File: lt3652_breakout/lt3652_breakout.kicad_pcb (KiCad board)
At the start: 2 copper layers, 37 parts, among them CON1 SLR PNL, U1 LT3652

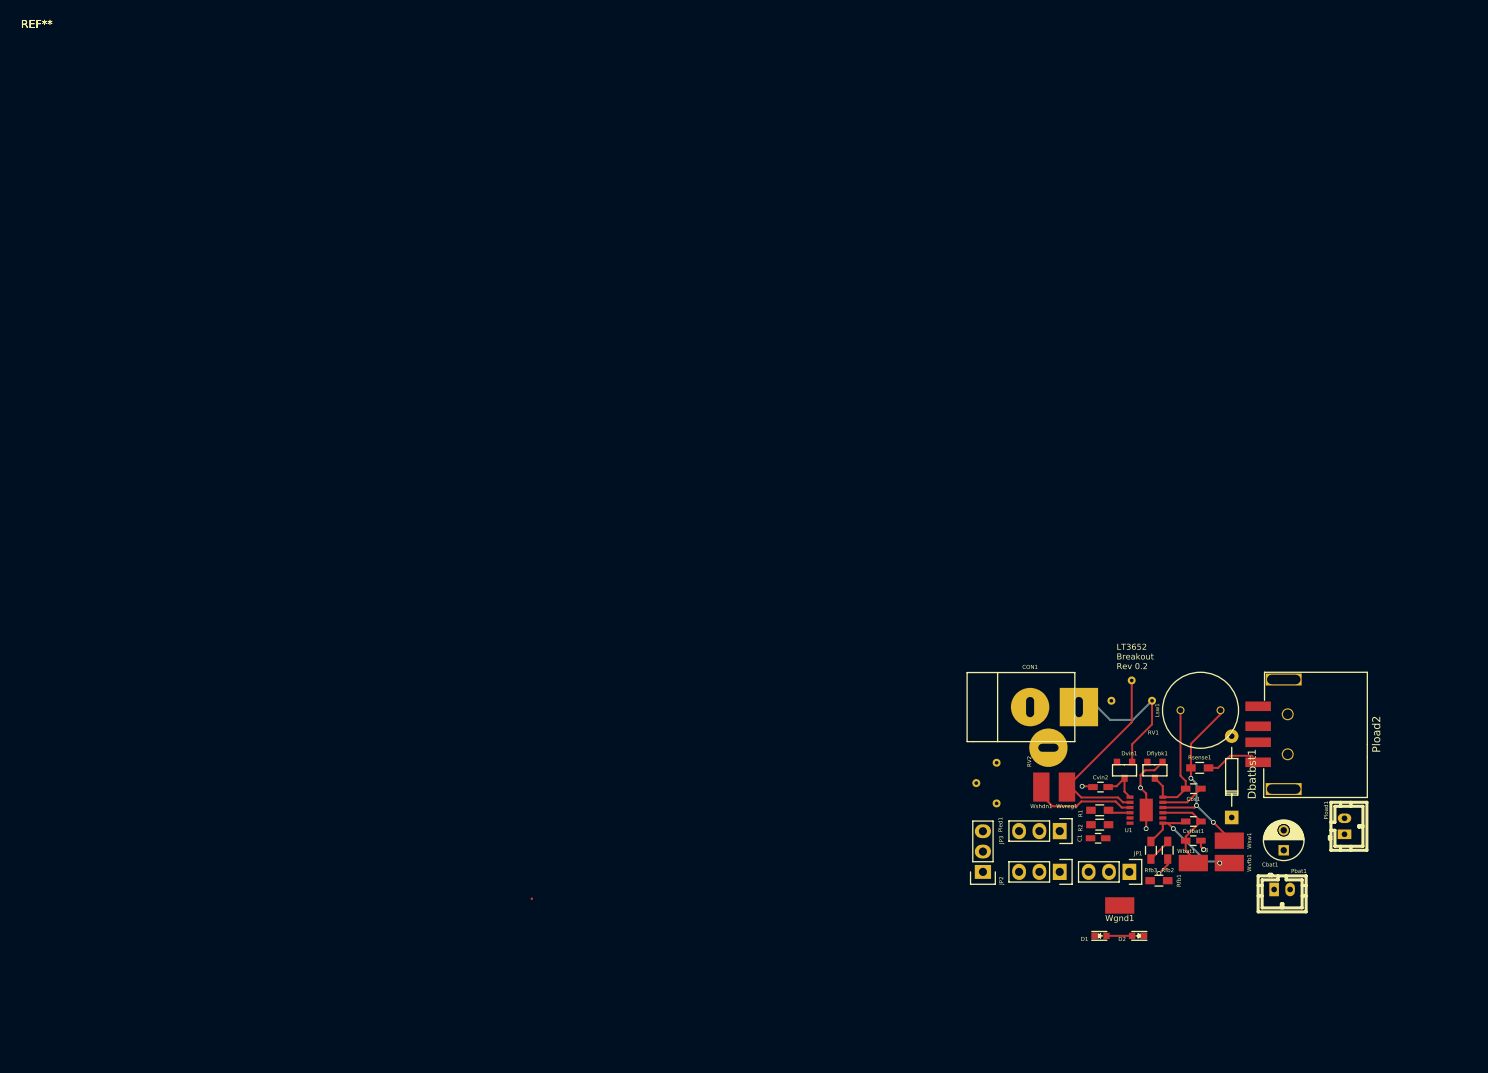
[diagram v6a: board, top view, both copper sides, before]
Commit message: Relaid pcb to the size of the box that will house it
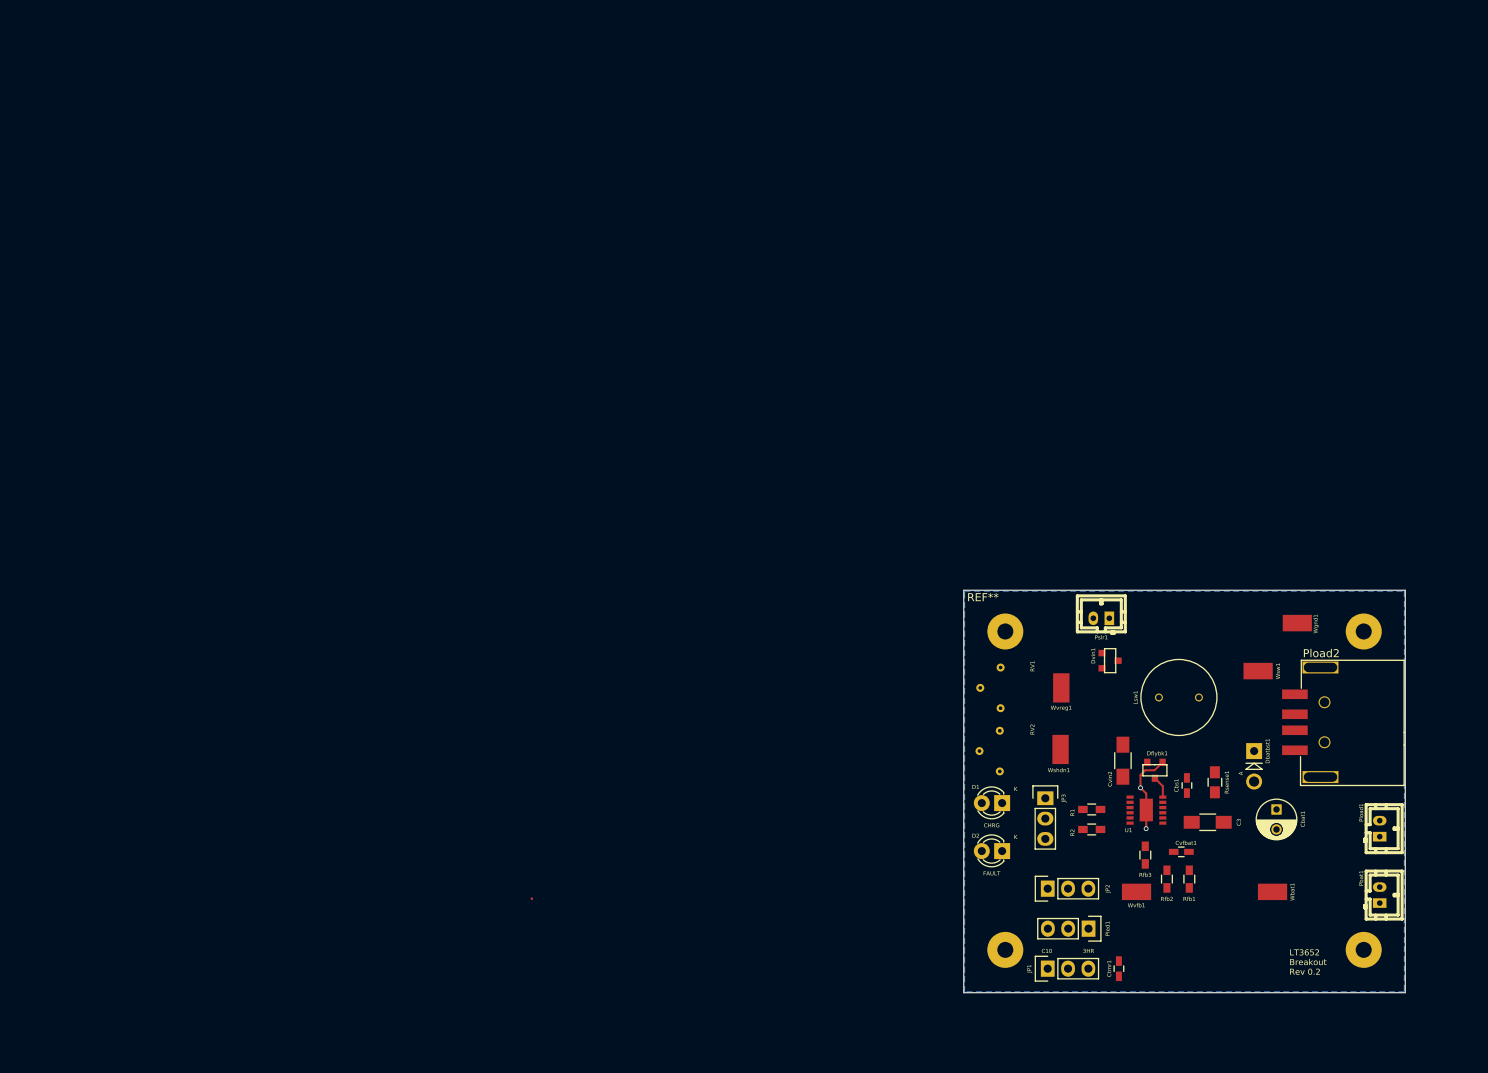
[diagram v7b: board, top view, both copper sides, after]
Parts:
- removed C1: C_Small, Capacitors_SMD:C_0603_HandSoldering
- removed CON1: SLR PNL, Connect:JACK_ALIM
- removed the REF** at (0.00, 0.00) (x2)
- added Ctmr1: 0.68µF, Capacitors_SMD:C_0603_HandSoldering, F.Cu at (135.3, 118.5)
- added Pslr1: JST PH, w_conn_jst-ph:b2b-ph-kl, F.Cu at (133.1, 74.8)
- added REF**: MHH-20_ABS_Plastic_Box, enclosures:MHH-20_ABS_Plastic_Box_Holes_Only, F.Cu at (143.9, 95.8)
- C3, Cvin2: footprint Capacitors_SMD:C_0603_HandSoldering -> Capacitors_SMD:C_1206_HandSoldering
- Cvfbat1: value 20pF -> 22pF
- D1, D2: footprint LEDs:LED_0603 -> LEDs:LED-3MM
- Dbatbst1: footprint Diodes_ThroughHole:Diode_DO-35_SOD27_Horizontal_RM10 -> Diodes_ThroughHole:Diode_DO-41_SOD81_Vertical_AnodeUp
- Rsense1: footprint Resistors_SMD:R_0603_HandSoldering -> Capacitors_SMD:C_0805_HandSoldering
- moved Wgnd1 41.7 mm to (157.6, 75.3), turned to 180 degrees
- moved Wsw1 21.5 mm to (152.7, 81.3)
- moved D1 20.7 mm to (120.7, 97.8), turned to 180 degrees
- moved D2 20.0 mm to (120.7, 103.8)
- moved RV1 16.5 mm to (120.5, 83.5), turned to 90 degrees
- moved JP1 15.8 mm to (126.4, 118.5), turned to 90 degrees
- moved Pled1 15.0 mm to (131.5, 113.5), turned to 270 degrees
- moved Dvin1 13.8 mm to (134.2, 80.0), turned to 270 degrees
- moved Wvreg1 12.4 mm to (128.1, 83.5), turned to 270 degrees
- moved Pbat1 12.2 mm to (167.9, 109.3), turned to 90 degrees
- moved Wvfb1 12.1 mm to (137.5, 109.0)
- moved Wbat1 10.5 mm to (154.5, 109.0)
- moved Dbatbst1 8.76 mm to (152.2, 91.3), turned to 270 degrees
- moved Wshdn1 5.28 mm to (128.0, 91.2), turned to 270 degrees
- moved Cbat1 5.18 mm to (155.0, 98.7), turned to 270 degrees
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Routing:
- net /VIN_REG: track 25.4 -> 0.00 mm
- net /SENSE: track 24.8 -> 0.00 mm, vias 3 -> 0
- net Net-(Dvin1-Pad3): track 19.5 -> 0.00 mm
- net /BAT: track 18.8 -> 0.00 mm
- net /VFB: track 16.2 -> 0.00 mm, vias 2 -> 0
- net /SW: track 16.1 -> 2.77 mm
- net /SHDN: track 13.2 -> 0.00 mm
- net GND: track 18.5 -> 10.4 mm, vias 5 -> 2
- net /BOOST: track 5.47 -> 0.00 mm
- net /VIN: track 5.11 -> 0.00 mm
- net Net-(Rfb1-Pad2): track 3.07 -> 0.00 mm
- net Net-(R1-Pad1): track 2.81 -> 0.00 mm
- added copper zone on B.Cu, net GND
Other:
- board outline added: 55.2 x 50.3 mm
- board text added: "3HR"
- board text added: "C10"
- board text added: "CHRG"
- board text added: "FAULT"

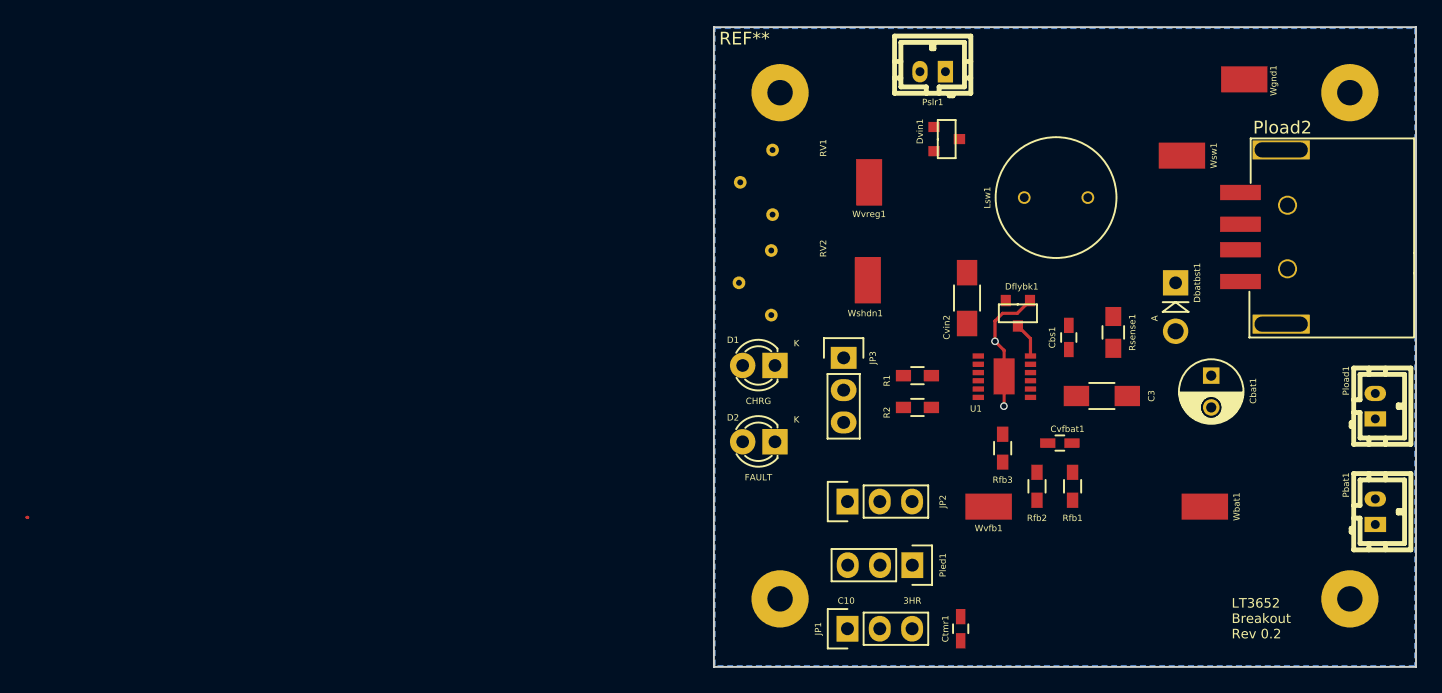
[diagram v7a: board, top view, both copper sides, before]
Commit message: Added option to connect load directly to Vin. Also routed the PCB
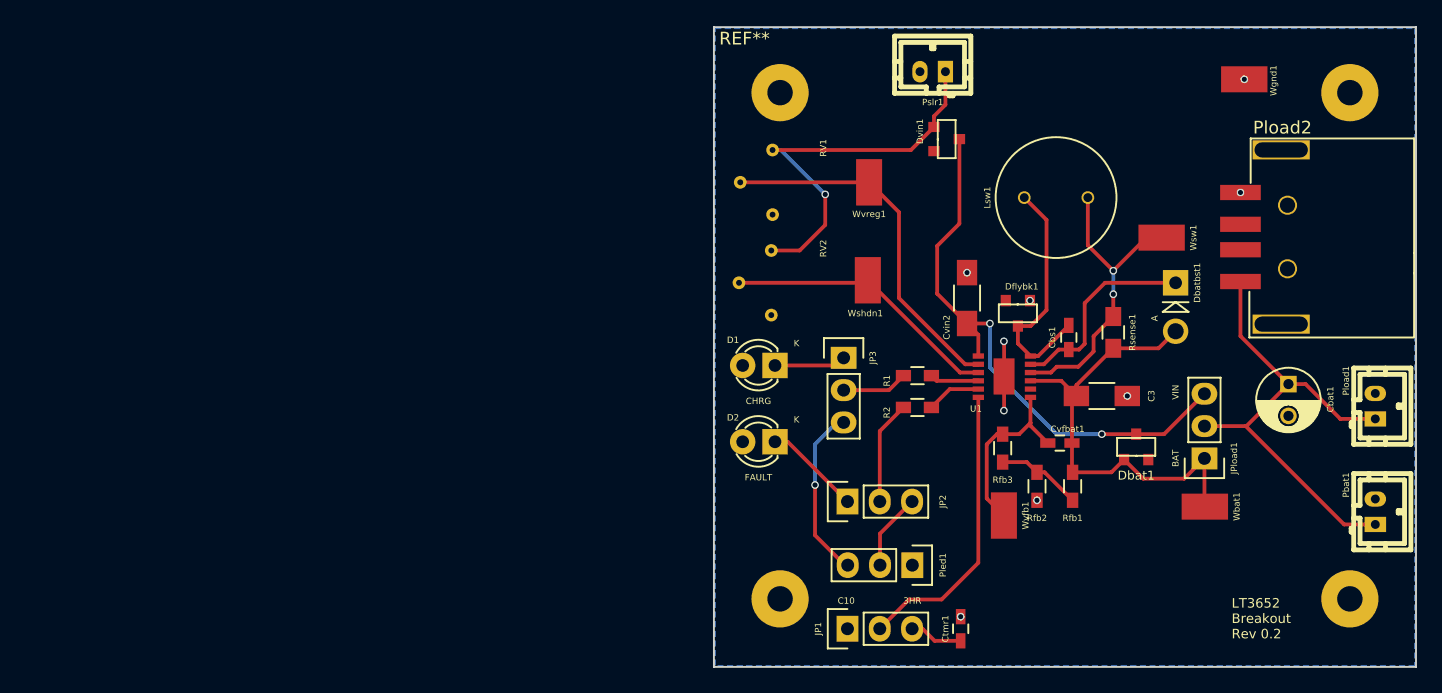
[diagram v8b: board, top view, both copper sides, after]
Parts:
- added Dbat1: D_Schottky_Small_ZLLS500, diodes:DIODES_INC_ZLLS500, F.Cu at (149.1, 104.2)
- added JPload1: JUMPER3, Pin_Headers:Pin_Header_Straight_1x03, F.Cu at (154.4, 105.2)
- moved Wsw1 6.65 mm to (151.1, 87.8)
- moved Cbat1 6.11 mm to (161.0, 99.3)
- moved Wvfb1 1.39 mm to (138.7, 109.7), turned to 90 degrees
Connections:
- Cbat1 pad 1: /BAT -> Net-(Cbat1-Pad1)
- Pbat1 pad 1: /BAT -> Net-(Cbat1-Pad1)
- Pload1 pad 1: /BAT -> Net-(Cbat1-Pad1)
- Pload2 pad 1: /BAT -> Net-(Cbat1-Pad1)
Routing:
- net /VIN: track 0.00 -> 44.7 mm, vias 0 -> 2
- net Net-(Cbat1-Pad1): track 0.00 -> 39.2 mm
- net /BAT: track 0.00 -> 36.5 mm
- net Net-(Dvin1-Pad3): track 0.00 -> 31.2 mm, vias 0 -> 1
- net /VIN_REG: track 0.00 -> 28.6 mm
- net /SENSE: track 0.00 -> 24.1 mm, vias 0 -> 2
- net Net-(JP1-Pad2): track 0.00 -> 22.9 mm
- net /SHDN: track 0.00 -> 21.9 mm
- net /SW: track 2.77 -> 19.2 mm
- net /BOOST: track 0.00 -> 15.9 mm
- net /VFB: track 0.00 -> 14.5 mm
- net Net-(JP3-Pad3): track 0.00 -> 13.7 mm, vias 0 -> 1
- net Net-(JP2-Pad2): track 0.00 -> 8.17 mm
- net Net-(D2-Pad1): track 0.00 -> 7.65 mm
- net Net-(Rfb1-Pad2): track 0.00 -> 6.74 mm
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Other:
- net class Power Traces added: clearance 0.3, trace_width 0.5, via_dia 0.8, via_drill 0.6
- board text added: "BAT"
- board text added: "VIN"
